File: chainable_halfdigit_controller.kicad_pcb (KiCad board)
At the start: 2 copper layers, 3 parts, among them J1 USB_OTG, U1 NRF24L01, U2 arduino_nano

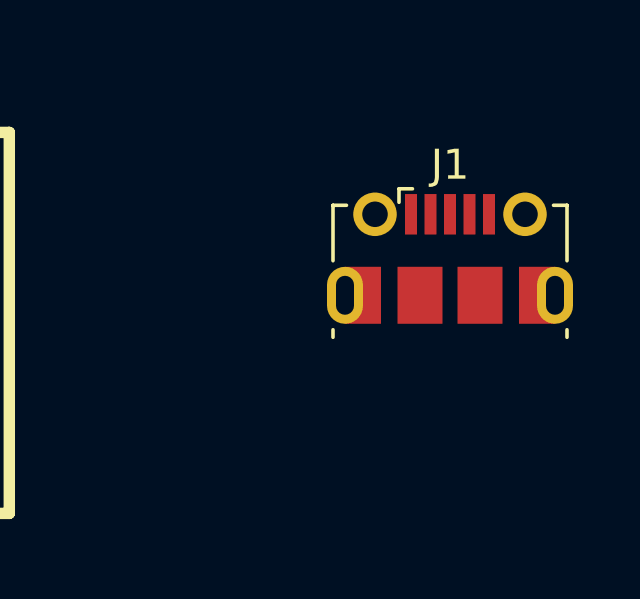
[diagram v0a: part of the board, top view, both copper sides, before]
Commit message: Made custom ST-USB-013A footprint for mini usb connector
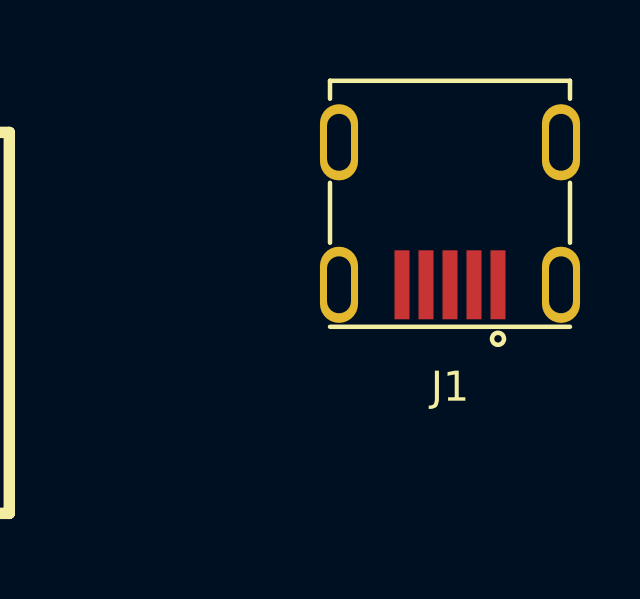
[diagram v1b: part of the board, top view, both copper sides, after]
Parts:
- J1: footprint Connectors_USB:USB_Micro-B_Molex-105017-0001 -> lib_fp:ST-USB-013A
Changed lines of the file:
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@@
 (kicad_pcb (version 4) (host pcbnew 4.0.7)
   (general
-    (links 18)
-    (no_connects 16)
-    (area 105.039499 83.257 167.925001 133.011001)
+    (links 14)
+    (no_connects 14)
+    (area 105.039499 82.175 167.835 133.011001)
     (thickness 1.6)
     (drawings 0)
@@
     (add_net SCK)
   )
-  (module Connectors_USB:USB_Micro-B_Molex-105017-0001 (layer F.Cu)
-    (at 163.3 90.95)
-    (descr http://www.molex.com/pdm_docs/sd/1050170001_sd.pdf)
-    (tags "Micro-USB SMD Typ-B")
-    (attr smd)
-    (fp_text reference J1 (at 0 -4) (layer F.SilkS)
-      (effects (font (size 1 1) (thickness 0.15)))
-    )
-    (fp_text value USB_OTG (at 0.3 3.45) (layer F.Fab)
-      (effects (font (size 1 1) (thickness 0.15)))
-    )
-    (fp_line (start -4.4 2.75) (end 4.4 2.75) (layer F.CrtYd) (width 0.05))
-    (fp_line (start 4.4 -3.35) (end 4.4 2.75) (layer F.CrtYd) (width 0.05))
-    (fp_line (start -4.4 -3.35) (end 4.4 -3.35) (layer F.CrtYd) (width 0.05))
-    (fp_line (start -4.4 2.75) (end -4.4 -3.35) (layer F.CrtYd) (width 0.05))
-    (fp_text user "PCB Edge" (at 0 1.8) (layer Dwgs.User)
-      (effects (font (size 0.5 0.5) (thickness 0.08)))
-    )
-    (fp_line (start -3.9 -2.65) (end -3.45 -2.65) (layer F.SilkS) (width 0.12))
-    (fp_line (start -3.9 -0.8) (end -3.9 -2.65) (layer F.SilkS) (width 0.12))
-    (fp_line (start 3.9 1.75) (end 3.9 1.5) (layer F.SilkS) (width 0.12))
-    (fp_line (start 3.75 2.5) (end 3.75 -2.5) (layer F.Fab) (width 0.1))
-    (fp_line (start -3 1.801704) (end 3 1.801704) (layer F.Fab) (width 0.1))
-    (fp_line (start -3.75 2.501704) (end 3.75 2.501704) (layer F.Fab) (width 0.1))
-    (fp_line (start -3.75 -2.5) (end 3.75 -2.5) (layer F.Fab) (width 0.1))
-    (fp_line (start -3.75 2.5) (end -3.75 -2.5) (layer F.Fab) (width 0.1))
-    (fp_line (start -3.9 1.75) (end -3.9 1.5) (layer F.SilkS) (width 0.12))
-    (fp_line (start 3.9 -0.8) (end 3.9 -2.65) (layer F.SilkS) (width 0.12))
-    (fp_line (start 3.9 -2.65) (end 3.45 -2.65) (layer F.SilkS) (width 0.12))
-    (fp_text user %R (at 0 0) (layer F.Fab)
-      (effects (font (size 1 1) (thickness 0.15)))
-    )
-    (fp_line (start -1.7 -3.2) (end -1.25 -3.2) (layer F.SilkS) (width 0.12))
-    (fp_line (start -1.7 -3.2) (end -1.7 -2.75) (layer F.SilkS) (width 0.12))
-    (fp_line (start -1.3 -2.6) (end -1.5 -2.8) (layer F.Fab) (width 0.1))
-    (fp_line (start -1.1 -2.8) (end -1.3 -2.6) (layer F.Fab) (width 0.1))
-    (fp_line (start -1.5 -3.01) (end -1.1 -3.01) (layer F.Fab) (width 0.1))
-    (fp_line (start -1.5 -3.01) (end -1.5 -2.8) (layer F.Fab) (width 0.1))
-    (fp_line (start -1.1 -3.01) (end -1.1 -2.8) (layer F.Fab) (width 0.1))
-    (pad 6 smd rect (at 1 0.35) (size 1.5 1.9) (layers F.Cu F.Paste F.Mask)
-      (net 1 GND))
-    (pad 6 thru_hole circle (at -2.5 -2.35) (size 1.45 1.45) (drill 0.85) (layers *.Cu *.Mask)
-      (net 1 GND))
-    (pad 2 smd rect (at -0.65 -2.35) (size 0.4 1.35) (layers F.Cu F.Paste F.Mask)
-      (net 2 "Net-(J1-Pad2)"))
-    (pad 1 smd rect (at -1.3 -2.35) (size 0.4 1.35) (layers F.Cu F.Paste F.Mask)
-      (net 3 5V))
-    (pad 5 smd rect (at 1.3 -2.35) (size 0.4 1.35) (layers F.Cu F.Paste F.Mask)
-      (net 1 GND))
-    (pad 4 smd rect (at 0.65 -2.35) (size 0.4 1.35) (layers F.Cu F.Paste F.Mask)
-      (net 4 "Net-(J1-Pad4)"))
-    (pad 3 smd rect (at 0 -2.35) (size 0.4 1.35) (layers F.Cu F.Paste F.Mask)
-      (net 5 "Net-(J1-Pad3)"))
-    (pad 6 thru_hole circle (at 2.5 -2.35) (size 1.45 1.45) (drill 0.85) (layers *.Cu *.Mask)
-      (net 1 GND))
-    (pad 6 smd rect (at -1 0.35) (size 1.5 1.9) (layers F.Cu F.Paste F.Mask)
-      (net 1 GND))
-    (pad 6 thru_hole oval (at -3.5 0.35 180) (size 1.2 1.9) (drill oval 0.6 1.3) (layers *.Cu *.Mask)
-      (net 1 GND))
-    (pad 6 thru_hole oval (at 3.5 0.35) (size 1.2 1.9) (drill oval 0.6 1.3) (layers *.Cu *.Mask)
-      (net 1 GND))
-    (pad 6 smd rect (at 2.9 0.35) (size 1.2 1.9) (layers F.Cu F.Mask)
-      (net 1 GND))
-    (pad 6 smd rect (at -2.9 0.35) (size 1.2 1.9) (layers F.Cu F.Mask)
-      (net 1 GND))
-    (model ${KISYS3DMOD}/Connectors_USB.3dshapes/USB_Micro-B_Molex-105017-0001.wrl
-      (at (xyz 0 0 0))
-      (scale (xyz 1 1 1))
-      (rotate (xyz 0 0 0))
-    )
-  )
   (module lib_fp:arduino_nano (layer F.Cu)
     (at 128.29 92.22)
@@
     )
   )
+  (module lib_fp:ST-USB-013A (layer F.Cu)
+    (at 163.3 90.95)
+    (fp_text reference J1 (at 0 3.4) (layer F.SilkS)
+      (effects (font (size 1 1) (thickness 0.15)))
+    )
+    (fp_text value USB_OTG (at -0.05 -7.8) (layer F.Fab)
+      (effects (font (size 1 1) (thickness 0.15)))
+    )
+    (fp_circle (center 1.6 1.8) (end 1.6 2) (layer F.SilkS) (width 0.15))
+    (fp_line (start 4 1.4) (end -4 1.4) (layer F.SilkS) (width 0.15))
+    (fp_line (start -4 -3.4) (end -4 -1.4) (layer F.SilkS) (width 0.15))
+    (fp_line (start 4 -3.4) (end 4 -1.4) (layer F.SilkS) (width 0.15))
+    (fp_line (start -4 -6.8) (end -4 -6.2) (layer F.SilkS) (width 0.15))
+    (fp_line (start 4 -6.8) (end 4 -6.2) (layer F.SilkS) (width 0.15))
+    (fp_line (start -4 -6.8) (end 4 -6.8) (layer F.SilkS) (width 0.15))
+    (pad 1 smd rect (at 1.6 0) (size 0.5 2.3) (layers F.Cu F.Paste F.Mask)
+      (net 3 5V))
+    (pad 2 smd rect (at 0.8 0) (size 0.5 2.3) (layers F.Cu F.Paste F.Mask)
+      (net 2 "Net-(J1-Pad2)"))
+    (pad 3 smd rect (at 0 0) (size 0.5 2.3) (layers F.Cu F.Paste F.Mask)
+      (net 5 "Net-(J1-Pad3)"))
+    (pad 4 smd rect (at -0.8 0) (size 0.5 2.3) (layers F.Cu F.Paste F.Mask)
+      (net 4 "Net-(J1-Pad4)"))
+    (pad 5 smd rect (at -1.6 0) (size 0.5 2.3) (layers F.Cu F.Paste F.Mask)
+      (net 1 GND))
+    (pad 6 thru_hole oval (at 3.7 0) (size 1.27 2.54) (drill oval 0.8 1.9) (layers *.Cu *.Mask)
+      (net 1 GND))
+    (pad 6 thru_hole oval (at -3.7 0) (size 1.27 2.54) (drill oval 0.8 1.9) (layers *.Cu *.Mask)
+      (net 1 GND))
+    (pad 6 thru_hole oval (at -3.7 -4.75) (size 1.27 2.54) (drill oval 0.8 1.9) (layers *.Cu *.Mask)
+      (net 1 GND))
+    (pad 6 thru_hole oval (at 3.7 -4.75) (size 1.27 2.54) (drill oval 0.8 1.9) (layers *.Cu *.Mask)
+      (net 1 GND))
+  )
 )

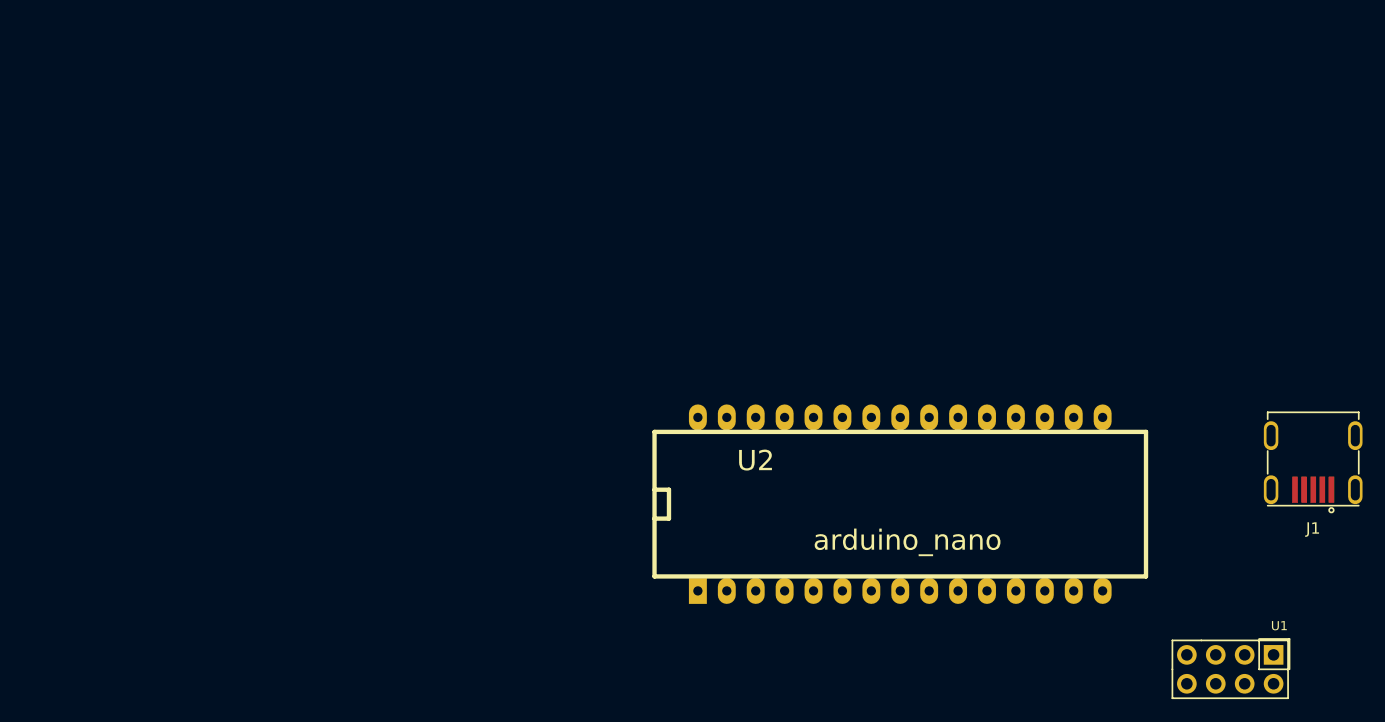
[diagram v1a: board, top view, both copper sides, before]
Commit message: Added bluetooth connection, board outline and mounting holes
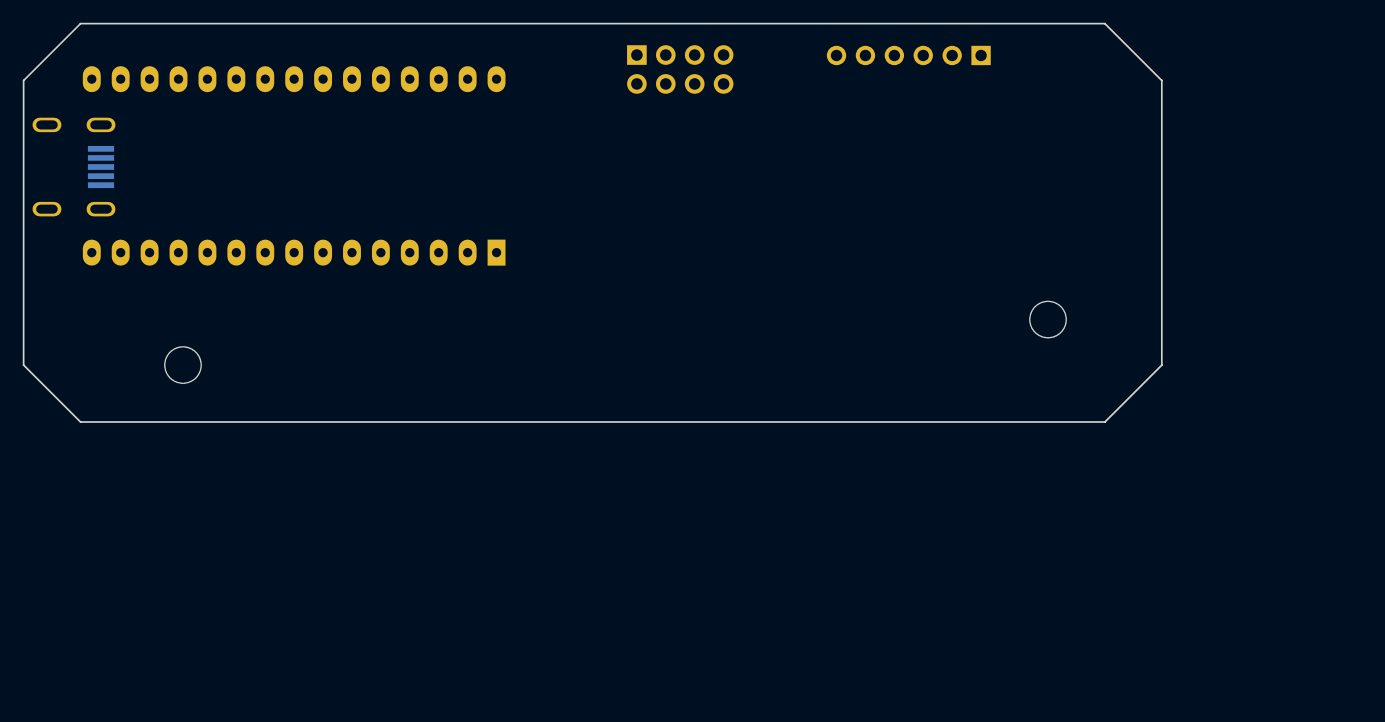
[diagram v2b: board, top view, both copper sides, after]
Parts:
- added J2: Conn_01x06, Socket_Strips:Socket_Strip_Angled_1x06_Pitch2.54mm, B.Cu at (134.1, 52.8)
- added REF**: MountingHole_3.2mm_M3, Mounting_Holes:MountingHole_3.2mm_M3, F.Cu at (64.0, 80.0)
- added REF**: MountingHole_3.2mm_M3, Mounting_Holes:MountingHole_3.2mm_M3, F.Cu at (140.0, 76.0)
- J1, U1, U2: moved to B.Cu
- moved J1 110.2 mm to (56.8, 62.6), turned to 270 degrees
- moved U1 79.1 mm to (102.4, 51.2), turned to 180 degrees
- moved U2 63.2 mm to (72.5, 62.5), turned to 180 degrees
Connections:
- net IRQ renamed Net-(U1-Pad8)
- U2 pad 22: Net-(U2-Pad22) -> BL_TXD
- U2 pad 23: Net-(U2-Pad23) -> BL_RXD
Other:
- board outline added: 100 x 35 mm

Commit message: Fixed ST-USB-013A pad sizes, added a mounting hole, added missing tracks
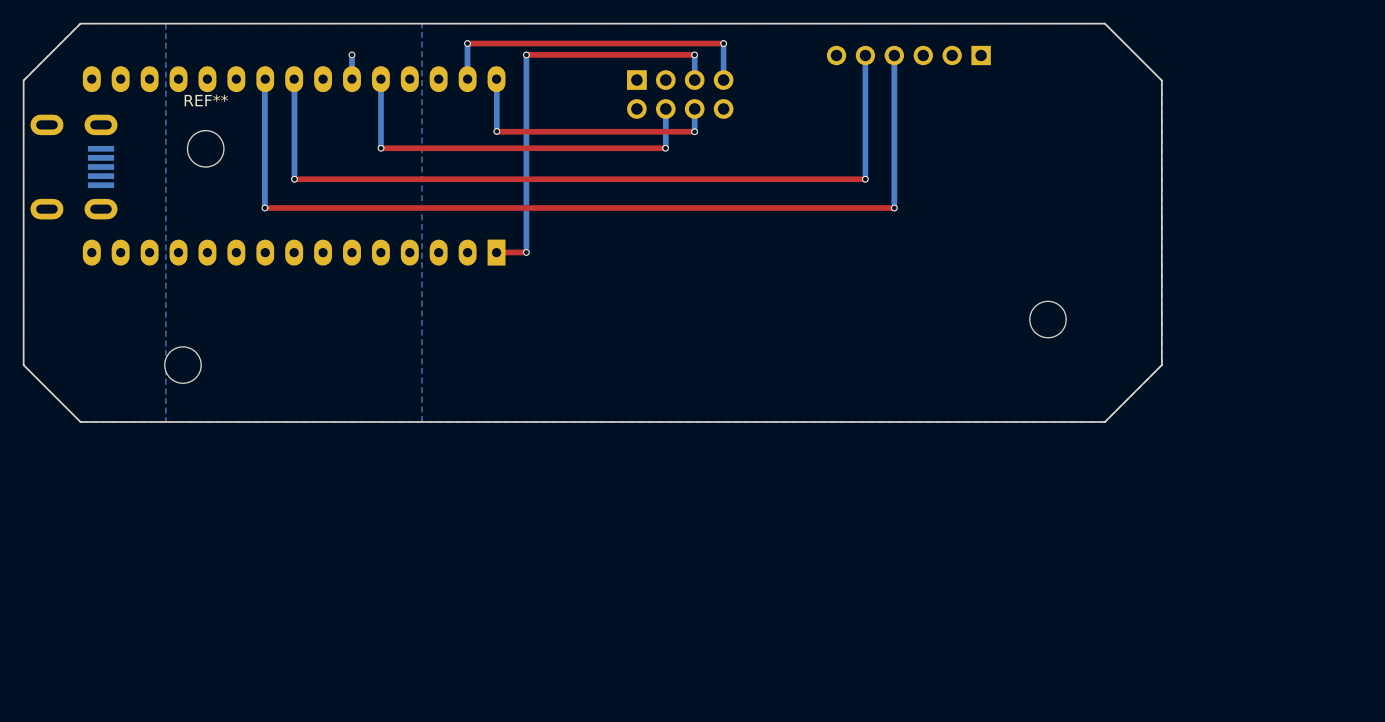
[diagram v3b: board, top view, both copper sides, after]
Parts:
- added REF**: MountingHole_3.2mm_M3, Mounting_Holes:MountingHole_3.2mm_M3, F.Cu at (66.0, 61.0)
- moved U1 2.20 mm to (102.4, 53.4)
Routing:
- net BL_TXD: track 0.00 -> 80.0 mm, vias 0 -> 2
- net BL_RXD: track 0.00 -> 69.8 mm, vias 0 -> 2
- net SCK: track 0.00 -> 37.0 mm, vias 0 -> 3
- net CSN: track 0.00 -> 34.5 mm, vias 0 -> 2
- net MISO: track 0.00 -> 29.2 mm, vias 0 -> 2
- net MOSI: track 0.00 -> 24.0 mm, vias 0 -> 2
- net CE: track 0.00 -> 2.13 mm, vias 0 -> 1
- added copper zone on B.Cu, net 3V3
- added copper zone on B.Cu, net 5V
- added copper zone on F.Cu, net GND
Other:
- net class DATA added: clearance 0.2, trace_width 0.5, via_dia 0.6, via_drill 0.4
- net class POWER added: clearance 0.2, trace_width 0.5, via_dia 0.6, via_drill 0.4

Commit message: Added info and logo, exported plot
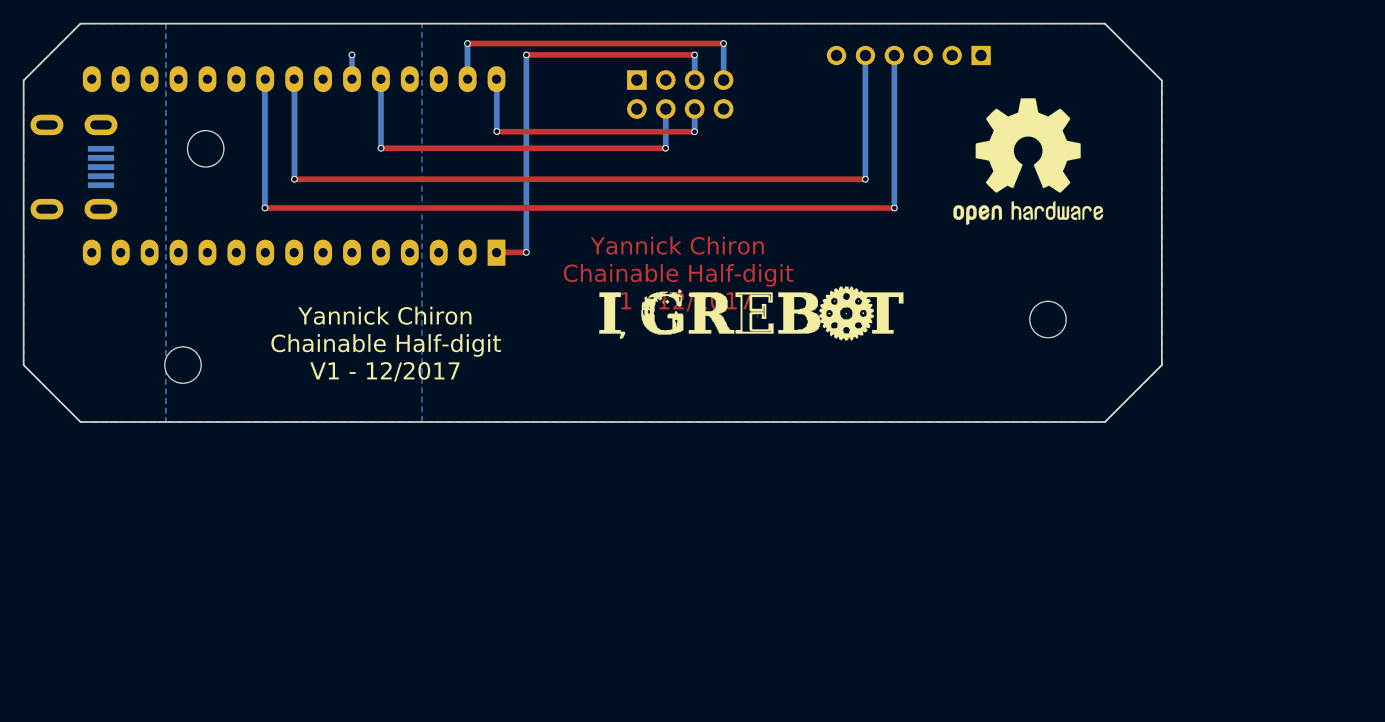
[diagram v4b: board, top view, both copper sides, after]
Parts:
- added G***: LOGO, lib_fp:logo_igrebot, F.Cu at (113.7, 74.9)
- added REF***: OSHW-Logo2_14.6x12mm_SilkScreen, Symbols:OSHW-Logo2_14.6x12mm_SilkScreen, F.Cu at (138.3, 62.1)
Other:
- board text added: "Yannick Chiron Chainable Half-digit V1 - 12/2017"

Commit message: Fixed card name
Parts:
- moved G*** 5.13 mm to (118.2, 72.5)
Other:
- board text added: "Yannick Chiron Chainable Half-digit controller V1 - 12/2017"
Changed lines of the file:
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@@
 (kicad_pcb (version 4) (host pcbnew 4.0.7)
   (general
-    (links 0)
+    (links 18)
     (no_connects 3)
     (area 49.924999 49.924999 150.075001 85.075001)
@@
   )
   (module lib_fp:logo_igrebot (layer F.Cu)
-    (at 113.67 74.93)
+    (at 118.16 72.45)
     (fp_text reference G*** (at 0 0) (layer F.SilkS) hide
       (effects (font (thickness 0.3)))
@@
       (xy -0.026262 -5.547126) (xy 0 -5.547126) (xy 0.209014 -5.547002)) (layer F.SilkS) (width 0.01))
   )
-  (gr_text "Yannick Chiron\nChainable Half-digit\nV1 - 12/2017" (at 81.82 78.15) (layer F.SilkS)
+  (gr_text "Yannick Chiron\nChainable Half-digit controller\nV1 - 12/2017" (at 86.66 78.76) (layer F.SilkS)
     (effects (font (size 1.5 1.5) (thickness 0.3)))
   )
